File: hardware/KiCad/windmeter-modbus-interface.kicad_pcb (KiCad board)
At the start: 2 copper layers, 70 x 92 mm, 30 parts, among them J1 MODBUS-P1, J2 Programming, J3 MODBUS-P2, J4 RJ14, J5 RJ14, U1 CH32V003J4M6, U2 MAX3485

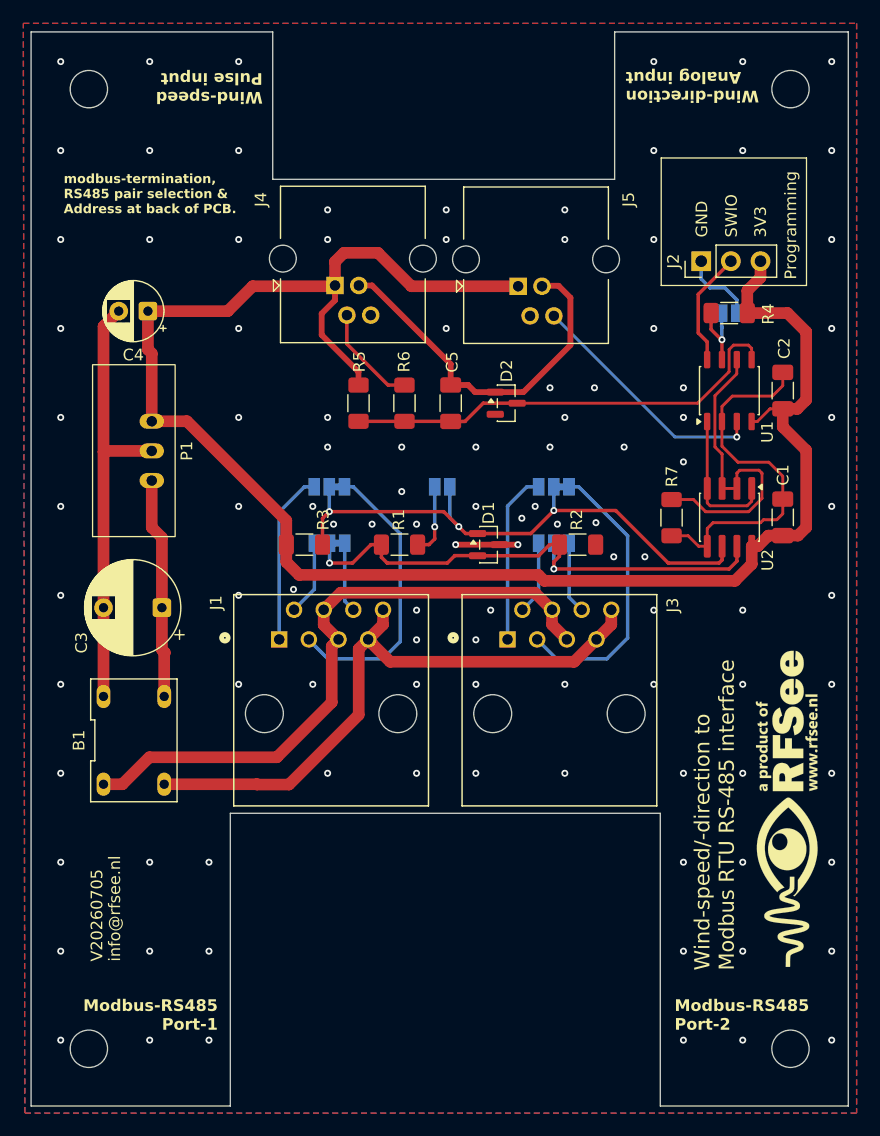
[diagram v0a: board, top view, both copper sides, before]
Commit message: FR-S40: runtime + persistent anemometer calibration (40005/40006)
Move the anemometer calibration from the compile-time-only WS_C_SCALED to
two persistent holding registers so one firmware image serves any
anemometer — no rebuild, calibrate over Modbus, survives power cycles.

- 40005 = calibration factor C (0.001 m/rotation, 1..6553, default 980),
  40006 = pulses per rotation (1..1000, default 1). Compile-time values are
  now the factory defaults; the running values are the registers.
- FR-S06 speed: count * C * 10 / (window_ms * pulses_per_rotation) — folds
  pulses/rotation into the divisor to keep full pulse resolution; ppr >= 1
  (holding min) guarantees no divide-by-zero.
- persist.c: record grew 16 -> 20 B (added ws_c/ws_ppr, crc span 14 -> 18),
  STORE_MAGIC 0x5747 -> 0x5748 so a pre-existing 4-register store cleanly
  re-defaults. persist_settings_t + load/save/verify extended.
- regs.c: the two holdings, accessors, persist wiring; a calibration change
  clears the averaging accumulator (FR-S30-style) so the boxcar never mixes
  scales — gated behind HAVE_WIND_SPEED so 40005/40006 stay inert on a
  direction-only build (FR-MB27).

Adversarial 3-lens review: flash-format + speed-formula clean; caught one
minor bug (cal write reset the direction average on a direction-only build)
— fixed (direction build shrank 44 B; combined unchanged).

Verified on the deployed combined unit @ 32: defaults [980,1], old store
re-defaulted, 40006 := 4 set live, range-rejects (exc 03), map edge 0x0006.

TDS -> v0.8 (FR-S40; FR-S06/FR-S25 reworked, FR-S39 now six registers,
§2.8 map extended). README/design/changelog/testReport updated.

Co-Authored-By: Claude Fable 5 <noreply@anthropic.com>
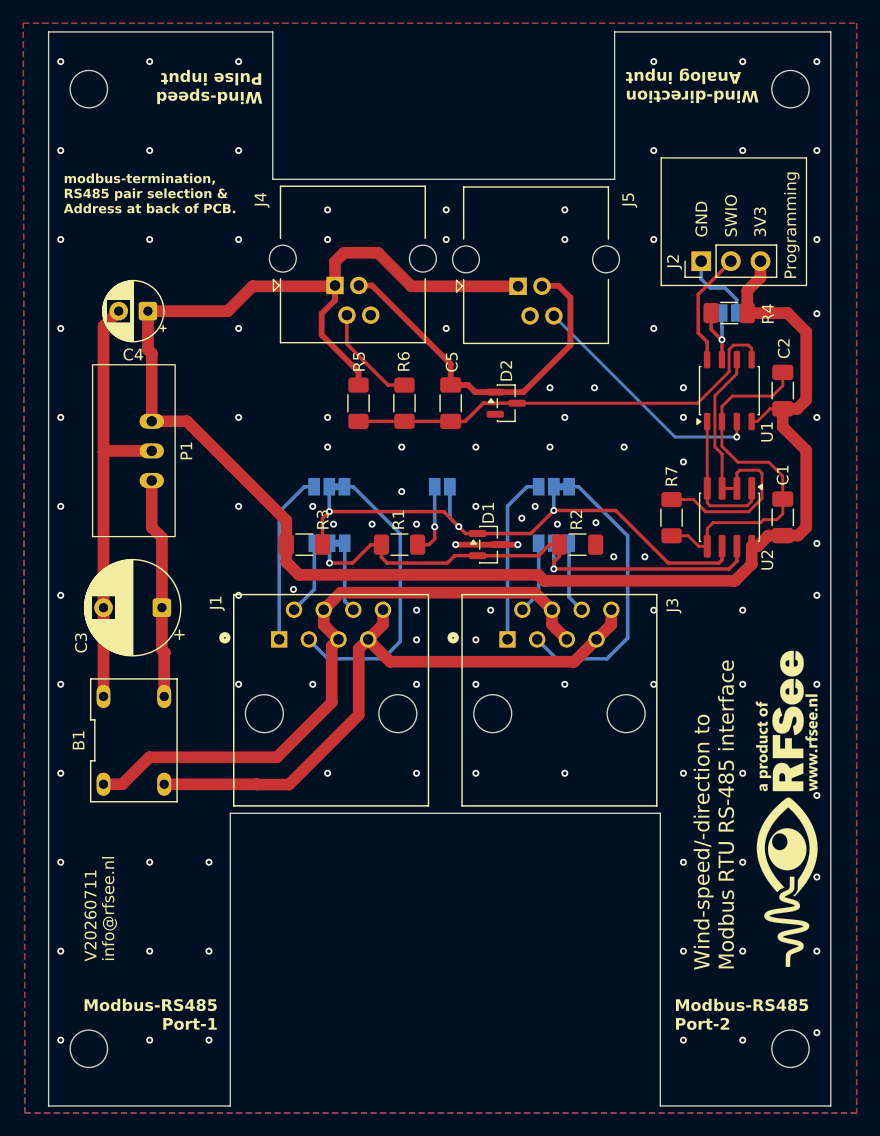
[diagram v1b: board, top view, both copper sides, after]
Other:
- board size 70 x 92 mm -> 67 x 92 mm
- board text added: "V20260711"
- board text removed: "V20260705"
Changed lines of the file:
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@@
 	(gr_poly
 		(pts
-			(xy 173.101 60.8844) (xy 202.386 60.8844) (xy 202.386 48.26) (xy 222.4 48.26) (xy 222.4 140.26) (xy 206.2976 140.26)
-			(xy 206.2976 115.1896) (xy 169.4676 115.1896) (xy 169.4676 140.26) (xy 152.4 140.26) (xy 152.4 48.26)
+			(xy 173.101 60.8844) (xy 202.386 60.8844) (xy 202.386 48.26) (xy 220.9 48.26) (xy 220.9 140.26) (xy 206.2976 140.26)
+			(xy 206.2976 115.1896) (xy 169.4676 115.1896) (xy 169.4676 140.26) (xy 153.9 140.26) (xy 153.9 48.26)
 			(xy 173.101 48.26)
 		)
@@
 		)
 	)
-	(gr_text "V20260705"
-		(at 158.623 127.889 90)
+	(gr_text "V20260711"
+		(at 158.115 127.889 90)
 		(layer "F.SilkS")
 		(effects
@@
 	)
 	(gr_text "info@rfsee.nl"
-		(at 160.147 127.889 90)
+		(at 159.639 127.889 90)
 		(layer "F.SilkS")
 		(effects
@@
 	)
 	(via
-		(at 220.98 104.14)
-		(size 0.6)
-		(drill 0.3)
-		(layers "F.Cu" "B.Cu")
-		(free yes)
-		(net "/GND")
-	)
-	(via
-		(at 220.98 96.52)
+		(at 219.71 104.14)
+		(size 0.6)
+		(drill 0.3)
+		(layers "F.Cu" "B.Cu")
+		(free yes)
+		(net "/GND")
+	)
+	(via
+		(at 219.71 96.52)
 		(size 0.6)
 		(drill 0.3)
@@
 	)
 	(via
-		(at 220.98 119.38)
+		(at 219.71 120.65)
 		(size 0.6)
 		(drill 0.3)
@@
 	)
 	(via
-		(at 220.98 81.28)
+		(at 219.71 81.28)
 		(size 0.6)
 		(drill 0.3)
@@
 	)
 	(via
-		(at 220.98 58.42)
+		(at 219.71 58.42)
 		(size 0.6)
 		(drill 0.3)
@@
 	)
 	(via
-		(at 220.98 134.62)
+		(at 219.71 133.985)
 		(size 0.6)
 		(drill 0.3)
@@
 	)
 	(via
-		(at 220.98 88.9)
+		(at 219.71 92.075)
 		(size 0.6)
 		(drill 0.3)
@@
 	)
 	(via
-		(at 220.98 50.8)
+		(at 219.71 50.8)
 		(size 0.6)
 		(drill 0.3)
@@
 	)
 	(via
-		(at 220.98 66.04)
+		(at 219.71 66.04)
 		(size 0.6)
 		(drill 0.3)
@@
 	)
 	(via
-		(at 220.98 111.76)
+		(at 219.71 113.665)
 		(size 0.6)
 		(drill 0.3)
@@
 	)
 	(via
-		(at 220.98 73.66)
+		(at 219.71 72.39)
 		(size 0.6)
 		(drill 0.3)
@@
 	)
 	(via
-		(at 220.98 127)
-		(size 0.6)
-		(drill 0.3)
+		(at 219.71 127)
+		(size 0.6)
+		(drill 0.3)
